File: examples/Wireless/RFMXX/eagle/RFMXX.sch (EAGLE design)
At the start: 5 parts

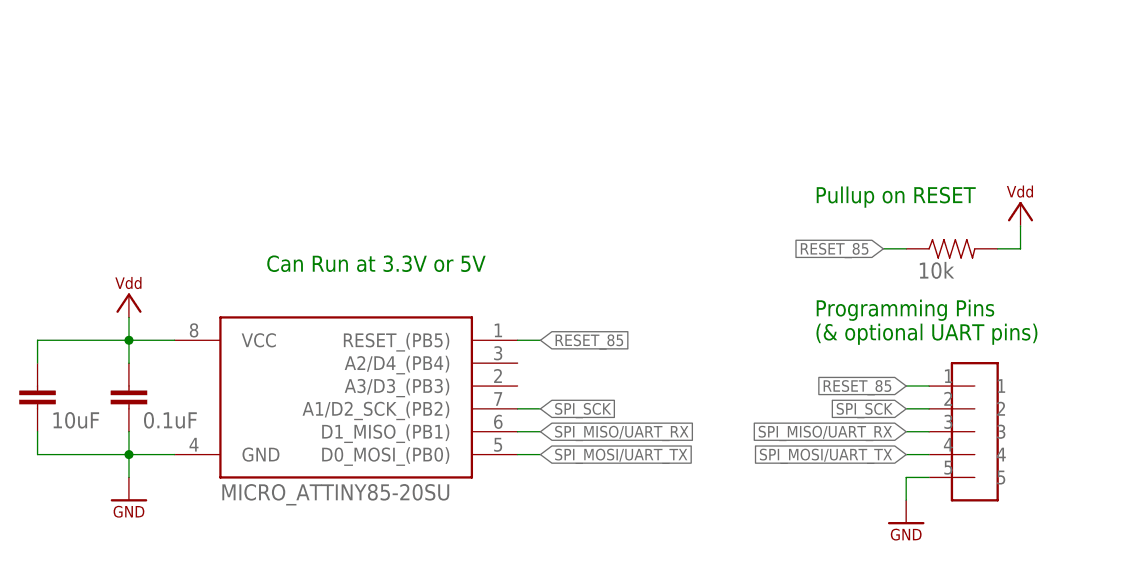
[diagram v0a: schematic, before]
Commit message: marquee template; schematic images
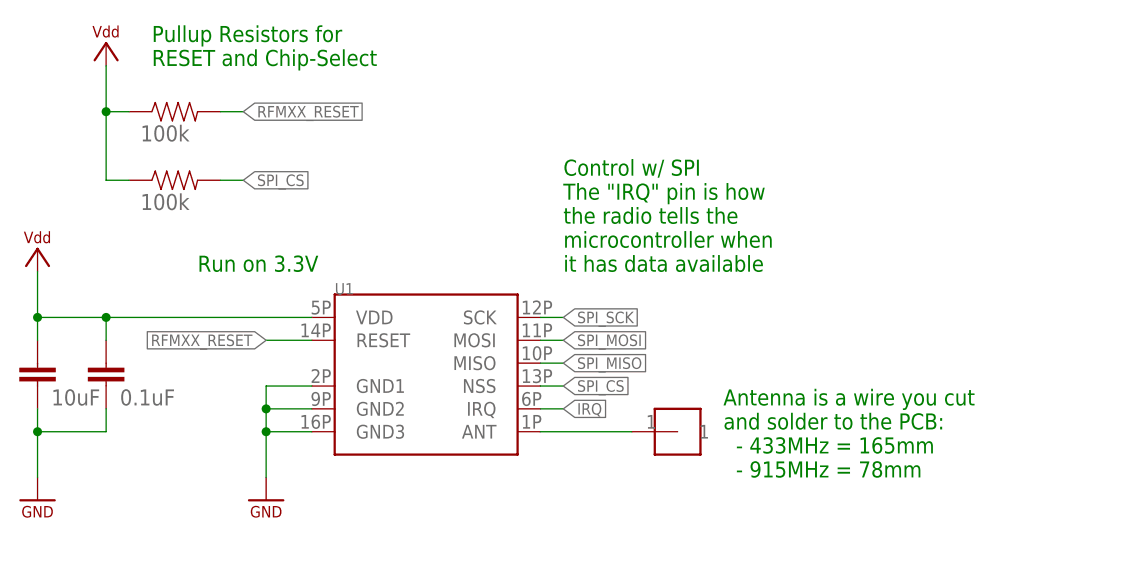
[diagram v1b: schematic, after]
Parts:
- removed U$2: HEADER-5-TESTPOINT, homemade-hardware:HEADER-5-TESTPOINT
- added R2: 100k, homemade-hardware:COMPONENT_RESISTOR-0805
- added U1: (no value), homemade-hardware:RADIO_RFMXX_SMT
- C1: value 0.1uF -> 10uF
- C2: value 10uF -> 0.1uF
- R1: value 10k -> 100k
- U$1: value MICRO_ATTINY85-20SU -> HEADER-1-DIP; device homemade-hardware:MICRO_ATTINY85-20SU -> homemade-hardware:HEADER-1-DIP
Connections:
- removed net RESET_85: R1.1, U$1.RESET_(PB5), U$2.1
- removed net SPI_MISO/UART_RX: U$1.D1_MISO_(PB1), U$2.3
- removed net SPI_MOSI/UART_TX: U$1.D0_MOSI_(PB0), U$2.4
- new net IRQ: U1.IRQ
- new net N$7: U$1.1, U1.ANT
- new net RFMXX_RESET: R2.2, U1.RESET
- new net SPI_CS: R1.2, U1.NSS
- new net SPI_MISO: U1.MISO
- new net SPI_MOSI: U1.MOSI
- net GND: now also U1.GND1, U1.GND2, U1.GND3; no longer U$1.GND, U$2.5
- net SPI_SCK: now also U1.SCK; no longer U$1.A1/D2_SCK_(PB2), U$2.2
- net VDD: now also R1.1, R2.1, U1.VDD; no longer R1.2, U$1.VCC
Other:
- note added: "Antenna is a wire you cut and solder to the PCB: - 433MHz = 165mm - 915MHz = 78mm"
- note added: "Control w/ SPI The "IRQ" pin is how the radio tells the microcontroller when it has data available"
- note added: "Pullup Resistors for RESET and Chip-Select"
- note added: "Run on 3.3V"
- note removed: "Can Run at 3.3V or 5V"
- note removed: "Programming Pins (& optional UART pins)"
- note removed: "Pullup on RESET"
